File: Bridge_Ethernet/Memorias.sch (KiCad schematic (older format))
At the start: 6 parts, among them U7 24LC256, U8 24LC256

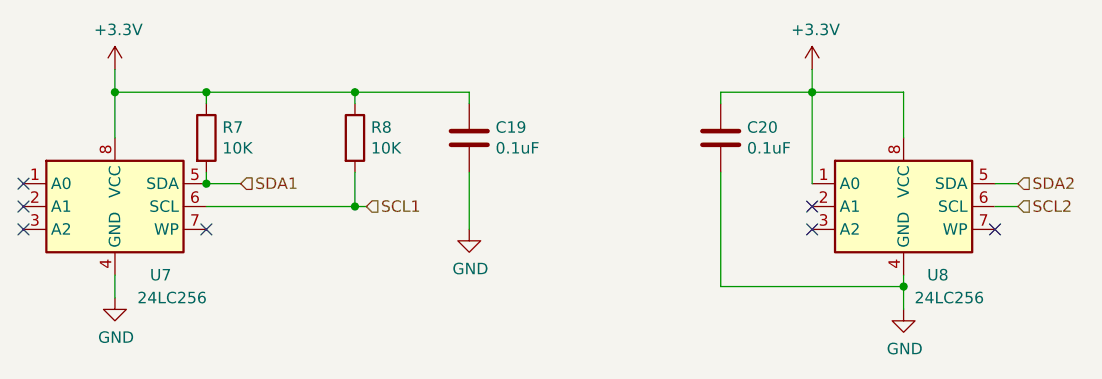
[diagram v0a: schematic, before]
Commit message: Esquemático Finalizado, sin warnings. Haciendo asignaciones de footprints
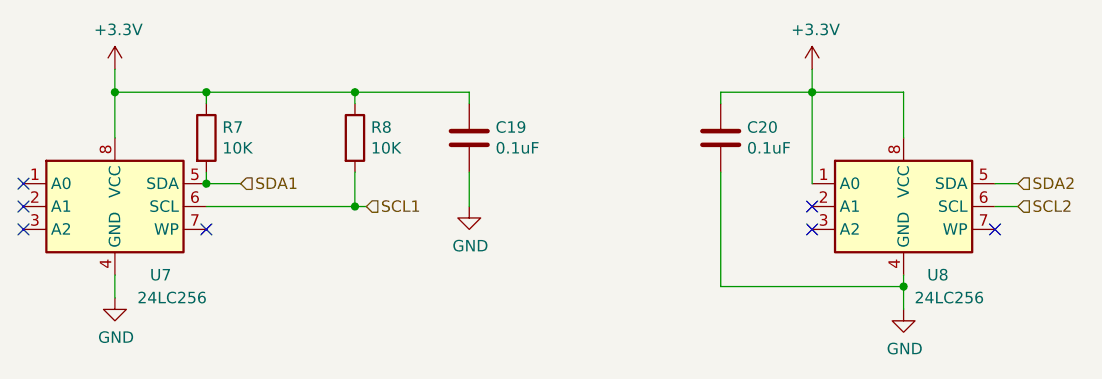
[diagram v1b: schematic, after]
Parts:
- U7, U8: footprint (none) -> 24LC256-E_SN:SOIC127P600X175-8N
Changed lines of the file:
@@
 $Descr A4 11693 8268
 encoding utf-8
-Sheet 5 9
+Sheet 4 9
 Title "Bridge Ethernet. Memorias."
 Date "2019-10-02"
@@
 F 0 "U7" H 4650 2000 50  0000 C CNN
 F 1 "24LC256" H 4700 1900 50  0000 C CNN
-F 2 "" H 4450 2300 50  0001 C CNN
+F 2 "24LC256-E_SN:SOIC127P600X175-8N" H 4450 2300 50  0001 C CNN
 F 3 "http://ww1.microchip.com/downloads/en/devicedoc/21203m.pdf" H 4450 2300 50  0001 C CNN
 	1    4450 2300
@@
 F 0 "U8" H 8050 2000 50  0000 C CNN
 F 1 "24LC256" H 8100 1900 50  0000 C CNN
-F 2 "" H 7900 2300 50  0001 C CNN
+F 2 "24LC256-E_SN:SOIC127P600X175-8N" H 7900 2300 50  0001 C CNN
 F 3 "http://ww1.microchip.com/downloads/en/devicedoc/21203m.pdf" H 7900 2300 50  0001 C CNN
 	1    7900 2300
@@
 L power:GND #PWR035
 U 1 1 5D96B661
-P 6000 2400
-F 0 "#PWR035" H 6000 2150 50  0001 C CNN
-F 1 "GND" H 6005 2227 50  0000 C CNN
-F 2 "" H 6000 2400 50  0001 C CNN
-F 3 "" H 6000 2400 50  0001 C CNN
-	1    6000 2400
-	1    0    0    -1
-$EndComp
-Wire Wire Line
-	6000 2400 6000 2150
+P 6000 2300
+F 0 "#PWR035" H 6000 2050 50  0001 C CNN
+F 1 "GND" H 6005 2127 50  0000 C CNN
+F 2 "" H 6000 2300 50  0001 C CNN
+F 3 "" H 6000 2300 50  0001 C CNN
+	1    6000 2300
+	1    0    0    -1
+$EndComp
 Wire Wire Line
 	4850 2200 5000 2200
@@
 Text HLabel 8400 2300 2    50   Input ~ 0
 SCL2
+Wire Wire Line
+	6000 2150 6000 2300
 $EndSCHEMATC

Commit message: Esquemático Finalizado. Asignaciones Realizadas. Comienzo de PCB.
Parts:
- C19, C20: footprint (none) -> Capacitor_SMD:C_0805_2012Metric
- R7, R8: footprint (none) -> Resistor_SMD:R_0805_2012Metric
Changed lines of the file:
@@
 F 0 "R7" H 4920 2046 50  0000 L CNN
 F 1 "10K" H 4920 1955 50  0000 L CNN
-F 2 "" V 4780 2000 50  0001 C CNN
+F 2 "Resistor_SMD:R_0805_2012Metric" V 4780 2000 50  0001 C CNN
 F 3 "~" H 4850 2000 50  0001 C CNN
 	1    4850 2000
@@
 F 0 "R8" H 5570 2046 50  0000 L CNN
 F 1 "10K" H 5570 1955 50  0000 L CNN
-F 2 "" V 5430 2000 50  0001 C CNN
+F 2 "Resistor_SMD:R_0805_2012Metric" V 5430 2000 50  0001 C CNN
 F 3 "~" H 5500 2000 50  0001 C CNN
 	1    5500 2000
@@
 F 0 "C19" H 6115 2046 50  0000 L CNN
 F 1 "0.1uF" H 6115 1955 50  0000 L CNN
-F 2 "" H 6038 1850 50  0001 C CNN
+F 2 "Capacitor_SMD:C_0805_2012Metric" H 6038 1850 50  0001 C CNN
 F 3 "~" H 6000 2000 50  0001 C CNN
 	1    6000 2000
@@
 F 0 "C20" H 7215 2046 50  0000 L CNN
 F 1 "0.1uF" H 7215 1955 50  0000 L CNN
-F 2 "" H 7138 1850 50  0001 C CNN
+F 2 "Capacitor_SMD:C_0805_2012Metric" H 7138 1850 50  0001 C CNN
 F 3 "~" H 7100 2000 50  0001 C CNN
 	1    7100 2000

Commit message: Esquemático Finalizado. Asignaciones Realizadas. Componentes acomodados en PCB.
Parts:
- renumbered C19 to C13, C20 to C14, R7 to R5, R8 to R6, U7 to U5, U8 to U6
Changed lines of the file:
@@
 $EndDescr
 $Comp
-L Memory_EEPROM:24LC256 U7
+L Memory_EEPROM:24LC256 U5
 U 1 1 5D95F943
 P 4450 2300
-F 0 "U7" H 4650 2000 50  0000 C CNN
+F 0 "U5" H 4650 2000 50  0000 C CNN
 F 1 "24LC256" H 4700 1900 50  0000 C CNN
 F 2 "24LC256-E_SN:SOIC127P600X175-8N" H 4450 2300 50  0001 C CNN
@@
 $EndComp
 $Comp
-L Memory_EEPROM:24LC256 U8
+L Memory_EEPROM:24LC256 U6
 U 1 1 5D960446
 P 7900 2300
-F 0 "U8" H 8050 2000 50  0000 C CNN
+F 0 "U6" H 8050 2000 50  0000 C CNN
 F 1 "24LC256" H 8100 1900 50  0000 C CNN
 F 2 "24LC256-E_SN:SOIC127P600X175-8N" H 7900 2300 50  0001 C CNN
@@
 NoConn ~ 4850 2400
 $Comp
-L power:+3.3V #PWR036
+L power:+3.3V #PWR024
 U 1 1 5D96119E
 P 7500 1700
-F 0 "#PWR036" H 7500 1550 50  0001 C CNN
+F 0 "#PWR024" H 7500 1550 50  0001 C CNN
 F 1 "+3.3V" H 7515 1873 50  0000 C CNN
 F 2 "" H 7500 1700 50  0001 C CNN
@@
 	8300 2200 8400 2200
 $Comp
-L power:GND #PWR037
+L power:GND #PWR025
 U 1 1 5D965839
 P 7900 2750
-F 0 "#PWR037" H 7900 2500 50  0001 C CNN
+F 0 "#PWR025" H 7900 2500 50  0001 C CNN
 F 1 "GND" H 7905 2577 50  0000 C CNN
 F 2 "" H 7900 2750 50  0001 C CNN
@@
 	7500 1800 7500 1700
 $Comp
-L power:+3.3V #PWR033
+L power:+3.3V #PWR021
 U 1 1 5D966F52
 P 4450 1700
-F 0 "#PWR033" H 4450 1550 50  0001 C CNN
+F 0 "#PWR021" H 4450 1550 50  0001 C CNN
 F 1 "+3.3V" H 4465 1873 50  0000 C CNN
 F 2 "" H 4450 1700 50  0001 C CNN
@@
 	4450 1800 4450 1700
 $Comp
-L Device:R R7
+L Device:R R5
 U 1 1 5D968008
 P 4850 2000
-F 0 "R7" H 4920 2046 50  0000 L CNN
+F 0 "R5" H 4920 2046 50  0000 L CNN
 F 1 "10K" H 4920 1955 50  0000 L CNN
 F 2 "Resistor_SMD:R_0805_2012Metric" V 4780 2000 50  0001 C CNN
@@
 	4850 1850 4850 1800
 $Comp
-L Device:R R8
+L Device:R R6
 U 1 1 5D9688A3
 P 5500 2000
-F 0 "R8" H 5570 2046 50  0000 L CNN
+F 0 "R6" H 5570 2046 50  0000 L CNN
 F 1 "10K" H 5570 1955 50  0000 L CNN
 F 2 "Resistor_SMD:R_0805_2012Metric" V 5430 2000 50  0001 C CNN
@@
 	5500 2150 5500 2300
 $Comp
-L Device:C C19
+L Device:C C13
 U 1 1 5D9692A4
 P 6000 2000
-F 0 "C19" H 6115 2046 50  0000 L CNN
+F 0 "C13" H 6115 2046 50  0000 L CNN
 F 1 "0.1uF" H 6115 1955 50  0000 L CNN
 F 2 "Capacitor_SMD:C_0805_2012Metric" H 6038 1850 50  0001 C CNN
@@
 	5500 1800 6000 1800
 $Comp
-L power:GND #PWR035
+L power:GND #PWR023
 U 1 1 5D96B661
 P 6000 2300
-F 0 "#PWR035" H 6000 2050 50  0001 C CNN
+F 0 "#PWR023" H 6000 2050 50  0001 C CNN
 F 1 "GND" H 6005 2127 50  0000 C CNN
 F 2 "" H 6000 2300 50  0001 C CNN
@@
 	4850 2300 5500 2300
 $Comp
-L Device:C C20
+L Device:C C14
 U 1 1 5D971F92
 P 7100 2000
-F 0 "C20" H 7215 2046 50  0000 L CNN
+F 0 "C14" H 7215 2046 50  0000 L CNN
 F 1 "0.1uF" H 7215 1955 50  0000 L CNN
 F 2 "Capacitor_SMD:C_0805_2012Metric" H 7138 1850 50  0001 C CNN
@@
 	7100 1800 7500 1800
 $Comp
-L power:GND #PWR034
+L power:GND #PWR022
 U 1 1 5D9622EF
 P 4450 2700
-F 0 "#PWR034" H 4450 2450 50  0001 C CNN
+F 0 "#PWR022" H 4450 2450 50  0001 C CNN
 F 1 "GND" H 4455 2527 50  0000 C CNN
 F 2 "" H 4450 2700 50  0001 C CNN
